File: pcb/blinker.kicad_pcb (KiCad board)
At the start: 2 copper layers, 55.9 x 55.9 mm, 14 parts, among them J1 ISP, U1 ATtiny10-TS

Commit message: Final PCB design?
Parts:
- moved D3 4.73 mm to (165.1, 76.2)
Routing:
- net 5VCC: track 49.6 -> 54.4 mm
- net /LED_R: track 12.4 -> 17.2 mm
- net GND: track 5.32 -> 8.23 mm
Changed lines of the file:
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@@
   )
   (footprint "LED_SMD:LED_0805_2012Metric" (layer "F.Cu")
-    (at 165.2525 80.93)
+    (at 165.1 76.2)
     (descr "LED SMD 0805 (2012 Metric), square (rectangular) end terminal, IPC_7351 nominal, (Body size source: https://docs.google.com/spreadsheets/d/1BsfQQcO9C6DZCsRaXUlFlo91Tg2WpOkGARC1WS5S8t0/edit?usp=sharing), generated with kicad-footprint-generator")
     (tags "LED")
@@
     (fp_line (start 8.471 6.568) (end 8.471 1.44) (layer "B.SilkS") (width 0.12))
     (fp_line (start 10.231 4.854) (end 10.231 -4.854) (layer "B.SilkS") (width 0.12))
+    (fp_line (start 10.991 3.637) (end 10.991 -3.637) (layer "B.SilkS") (width 0.12))
     (fp_line (start 6.311 -1.44) (end 6.311 -7.666) (layer "B.SilkS") (width 0.12))
     (fp_line (start 9.231 5.952) (end 9.231 -5.952) (layer "B.SilkS") (width 0.12))
@@
     (fp_line (start 7.151 7.334) (end 7.151 1.44) (layer "B.SilkS") (width 0.12))
     (fp_line (start 5.951 7.777) (end 5.951 -7.777) (layer "B.SilkS") (width 0.12))
-    (fp_line (start 10.991 3.637) (end 10.991 -3.637) (layer "B.SilkS") (width 0.12))
     (fp_line (start 8.991 6.163) (end 8.991 -6.163) (layer "B.SilkS") (width 0.12))
     (fp_line (start 7.511 7.157) (end 7.511 1.44) (layer "B.SilkS") (width 0.12))
@@
   )
   (segment (start 158.05 93.79) (end 158.05 97.56) (width 0.25) (layer "F.Cu") (net 1))
-  (segment (start 173.38 99.28) (end 172.014511 100.645489) (width 0.25) (layer "F.Cu") (net 2))
-  (segment (start 172.014511 100.645489) (end 168.625489 100.645489) (width 0.25) (layer "F.Cu") (net 2))
+  (segment (start 168.914511 100.454511) (end 168.33 99.87) (width 0.25) (layer "F.Cu") (net 2))
+  (segment (start 172.205489 100.454511) (end 168.914511 100.454511) (width 0.25) (layer "F.Cu") (net 2))
+  (segment (start 173.38 99.28) (end 172.205489 100.454511) (width 0.25) (layer "F.Cu") (net 2))
+  (segment (start 168.33 99.87) (end 165.88 99.87) (width 0.25) (layer "F.Cu") (net 2))
   (segment (start 165.88 101.94) (end 170.84 106.9) (width 0.25) (layer "F.Cu") (net 3))
   (segment (start 165.88 100.82) (end 165.88 101.94) (width 0.25) (layer "F.Cu") (net 3))
@@
   (segment (start 158.05 88.971773) (end 157.48 88.401773) (width 0.25) (layer "F.Cu") (net 9))
   (segment (start 149.86 101.6) (end 149.86 107.178227) (width 0.25) (layer "F.Cu") (net 9))
-  (segment (start 164.315 93.085) (end 164.485 93.255) (width 0.25) (layer "F.Cu") (net 10))
-  (segment (start 164.315 80.93) (end 164.315 93.085) (width 0.25) (layer "F.Cu") (net 10))
+  (segment (start 164.485 93.255) (end 164.485 76.5225) (width 0.25) (layer "F.Cu") (net 10))
+  (segment (start 164.485 76.5225) (end 164.1625 76.2) (width 0.25) (layer "F.Cu") (net 10))
   (segment (start 166.6 108.24) (end 172.04 108.24) (width 0.25) (layer "F.Cu") (net 11))
+  (segment (start 167 91.59) (end 167 77.1625) (width 0.25) (layer "F.Cu") (net 11))
   (segment (start 163.605 99.87) (end 163.221428 99.87) (width 0.25) (layer "F.Cu") (net 11))
+  (segment (start 167 77.1625) (end 166.0375 76.2) (width 0.25) (layer "F.Cu") (net 11))
   (segment (start 162.61798 100.473448) (end 162.61798 104.25798) (width 0.25) (layer "F.Cu") (net 11))
   (segment (start 166.6 108.24) (end 165.75 107.39) (width 0.25) (layer "F.Cu") (net 11))
   (segment (start 162.61798 104.25798) (end 165.75 107.39) (width 0.25) (layer "F.Cu") (net 11))
-  (segment (start 166.19 80.93) (end 167 81.74) (width 0.25) (layer "F.Cu") (net 11))
-  (segment (start 167 81.74) (end 167 91.59) (width 0.25) (layer "F.Cu") (net 11))
   (segment (start 172.04 108.24) (end 173.38 106.9) (width 0.25) (layer "F.Cu") (net 11))
   (segment (start 163.221428 99.87) (end 162.61798 100.473448) (width 0.25) (layer "F.Cu") (net 11))

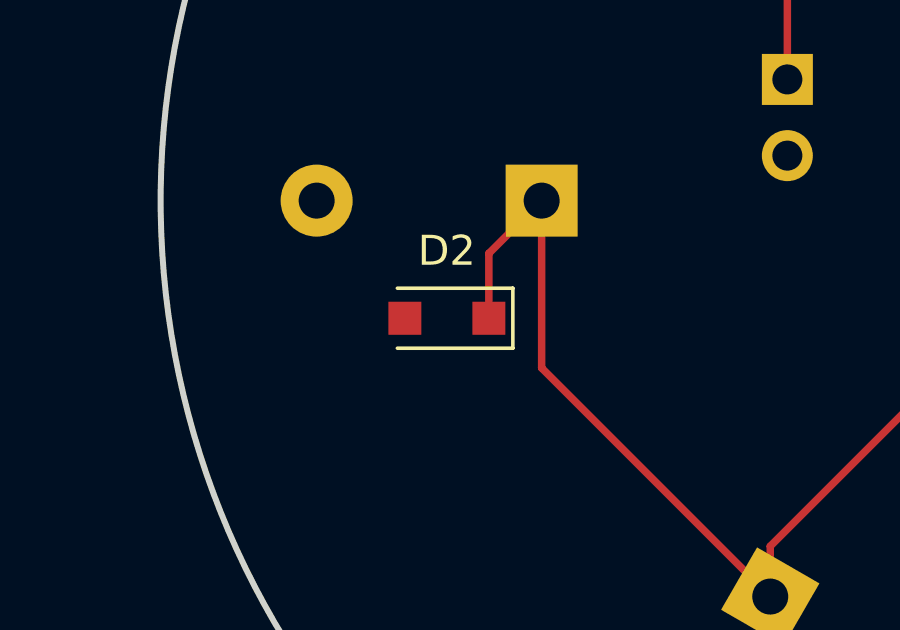
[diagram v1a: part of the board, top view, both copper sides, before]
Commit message: Fix zener selection.
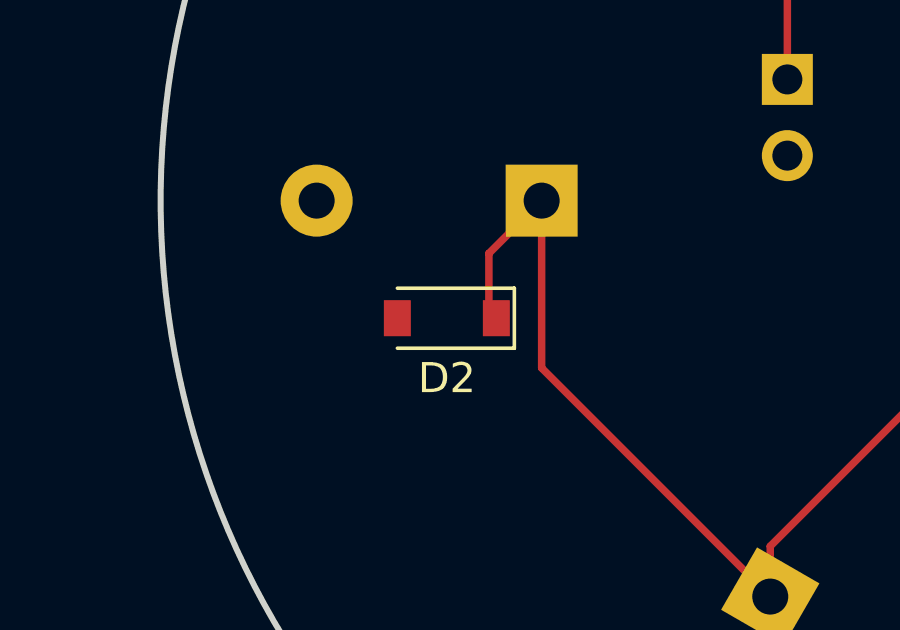
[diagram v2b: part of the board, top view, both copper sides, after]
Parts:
- D2: footprint Diode_SMD:D_SOD-123F -> Diode_SMD:D_SOD-123
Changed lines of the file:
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@@
   (net 11 "5VCC")
   (net 12 "LED")
-  (footprint "Diode_SMD:D_SOD-123F" (layer "F.Cu")
+  (footprint "Diode_SMD:D_SOD-123" (layer "F.Cu")
     (at 146.7 105.52 180)
-    (descr "D_SOD-123F")
-    (tags "D_SOD-123F")
-    (property "LCSC" "C362294")
+    (descr "SOD-123")
+    (tags "SOD-123")
+    (property "LCSC" "C96629")
     (property "Sheetfile" "blinker.kicad_sch")
     (property "Sheetname" "")
     (attr smd)
-    (fp_text reference "D2" (at 0.005 2.245) (layer "F.SilkS")
+    (fp_text reference "D2" (at 0 -2 180) (layer "F.SilkS")
       (effects (font (size 1 1) (thickness 0.15)))
     )
-    (fp_text value "D_Zener" (at 0 2.1) (layer "F.Fab")
+    (fp_text value "D_Zener" (at 0 2.1 180) (layer "F.Fab")
       (effects (font (size 1 1) (thickness 0.15)))
     )
-    (fp_text user "${REFERENCE}" (at -0.127 -1.905) (layer "F.Fab")
+    (fp_text user "${REFERENCE}" (at 0 -2 180) (layer "F.Fab")
       (effects (font (size 1 1) (thickness 0.15)))
     )
-    (fp_line (start -2.2 -1) (end -2.2 1) (layer "F.SilkS") (width 0.12))
-    (fp_line (start -2.2 1) (end 1.65 1) (layer "F.SilkS") (width 0.12))
-    (fp_line (start -2.2 -1) (end 1.65 -1) (layer "F.SilkS") (width 0.12))
-    (fp_line (start -2.2 -1.15) (end -2.2 1.15) (layer "F.CrtYd") (width 0.05))
-    (fp_line (start 2.2 -1.15) (end 2.2 1.15) (layer "F.CrtYd") (width 0.05))
-    (fp_line (start 2.2 1.15) (end -2.2 1.15) (layer "F.CrtYd") (width 0.05))
-    (fp_line (start -2.2 -1.15) (end 2.2 -1.15) (layer "F.CrtYd") (width 0.05))
-    (fp_line (start 0.25 0.4) (end -0.35 0) (layer "F.Fab") (width 0.1))
+    (fp_line (start -2.25 1) (end 1.65 1) (layer "F.SilkS") (width 0.12))
+    (fp_line (start -2.25 -1) (end -2.25 1) (layer "F.SilkS") (width 0.12))
+    (fp_line (start -2.25 -1) (end 1.65 -1) (layer "F.SilkS") (width 0.12))
+    (fp_line (start -2.35 -1.15) (end 2.35 -1.15) (layer "F.CrtYd") (width 0.05))
+    (fp_line (start 2.35 1.15) (end -2.35 1.15) (layer "F.CrtYd") (width 0.05))
+    (fp_line (start 2.35 -1.15) (end 2.35 1.15) (layer "F.CrtYd") (width 0.05))
+    (fp_line (start -2.35 -1.15) (end -2.35 1.15) (layer "F.CrtYd") (width 0.05))
+    (fp_line (start -0.35 0) (end -0.35 0.55) (layer "F.Fab") (width 0.1))
     (fp_line (start -0.35 0) (end 0.25 -0.4) (layer "F.Fab") (width 0.1))
+    (fp_line (start -0.75 0) (end -0.35 0) (layer "F.Fab") (width 0.1))
+    (fp_line (start 1.4 0.9) (end -1.4 0.9) (layer "F.Fab") (width 0.1))
     (fp_line (start -0.35 0) (end -0.35 -0.55) (layer "F.Fab") (width 0.1))
-    (fp_line (start -0.35 0) (end -0.35 0.55) (layer "F.Fab") (width 0.1))
-    (fp_line (start -0.75 0) (end -0.35 0) (layer "F.Fab") (width 0.1))
     (fp_line (start -1.4 -0.9) (end 1.4 -0.9) (layer "F.Fab") (width 0.1))
     (fp_line (start 0.25 -0.4) (end 0.25 0.4) (layer "F.Fab") (width 0.1))
+    (fp_line (start -1.4 0.9) (end -1.4 -0.9) (layer "F.Fab") (width 0.1))
     (fp_line (start 0.25 0) (end 0.75 0) (layer "F.Fab") (width 0.1))
     (fp_line (start 1.4 -0.9) (end 1.4 0.9) (layer "F.Fab") (width 0.1))
-    (fp_line (start 1.4 0.9) (end -1.4 0.9) (layer "F.Fab") (width 0.1))
-    (fp_line (start -1.4 0.9) (end -1.4 -0.9) (layer "F.Fab") (width 0.1))
-    (pad "1" smd rect (at -1.4 0 180) (size 1.1 1.1) (layers "F.Cu" "F.Paste" "F.Mask")
+    (fp_line (start 0.25 0.4) (end -0.35 0) (layer "F.Fab") (width 0.1))
+    (pad "1" smd rect (at -1.65 0 180) (size 0.9 1.2) (layers "F.Cu" "F.Paste" "F.Mask")
       (net 9 "2.7VCC") (pinfunction "K") (pintype "passive"))
-    (pad "2" smd rect (at 1.4 0 180) (size 1.1 1.1) (layers "F.Cu" "F.Paste" "F.Mask")
+    (pad "2" smd rect (at 1.65 0 180) (size 0.9 1.2) (layers "F.Cu" "F.Paste" "F.Mask")
       (net 2 "GND") (pinfunction "A") (pintype "passive"))
-    (model "${KICAD6_3DMODEL_DIR}/Diode_SMD.3dshapes/D_SOD-123F.wrl"
+    (model "${KICAD6_3DMODEL_DIR}/Diode_SMD.3dshapes/D_SOD-123.wrl"
       (offset (xyz 0 0 0))
       (scale (xyz 1 1 1))

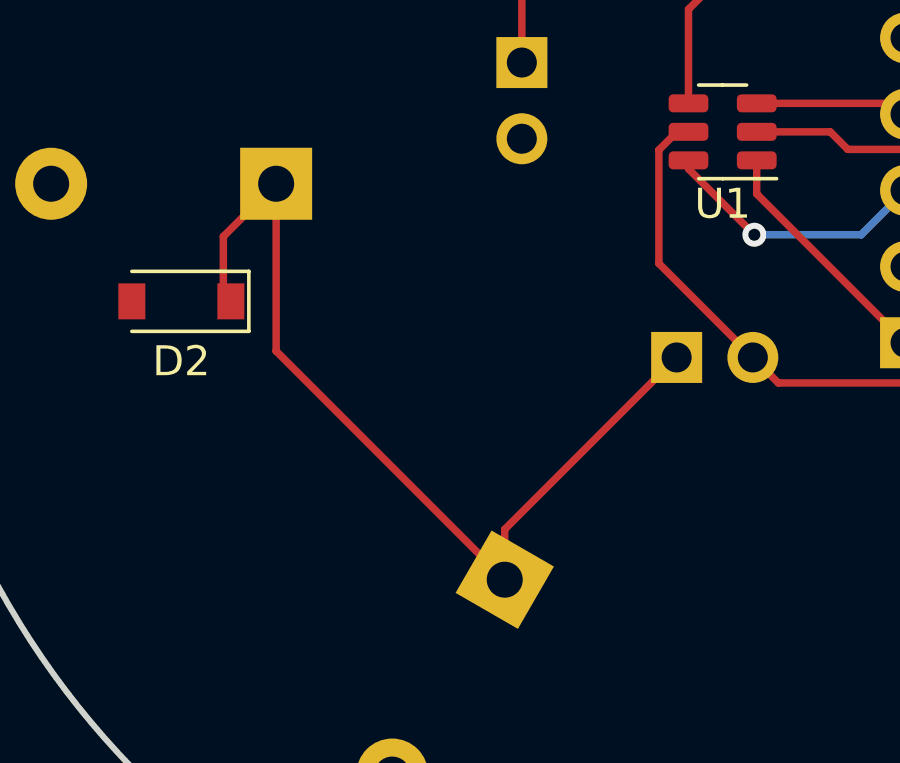
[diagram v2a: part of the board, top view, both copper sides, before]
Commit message: Gotta fix the rotation on U1.
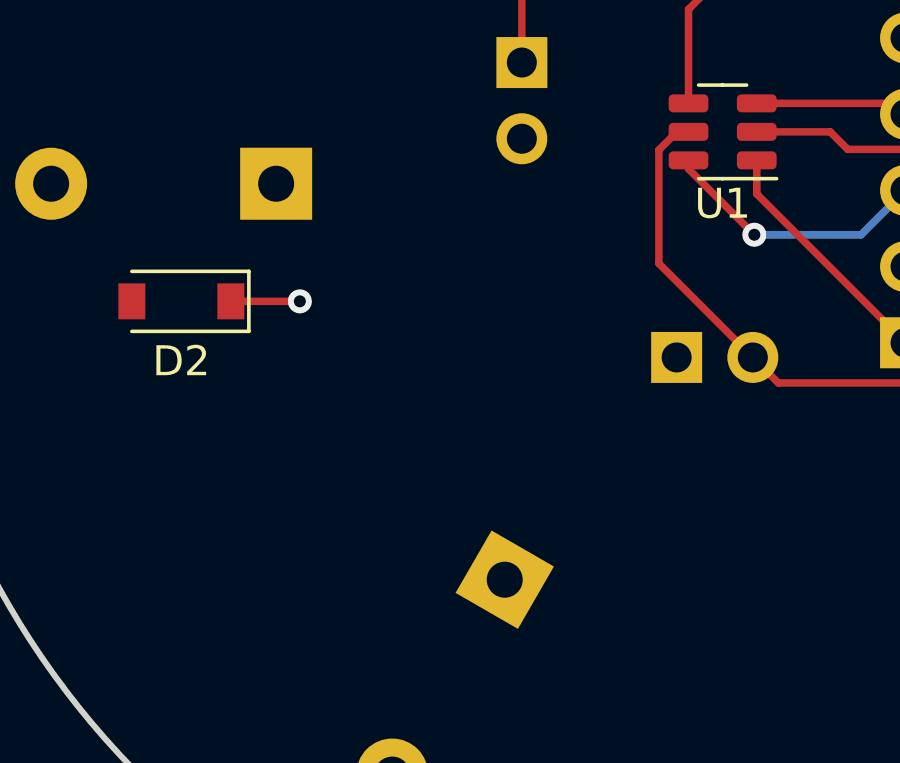
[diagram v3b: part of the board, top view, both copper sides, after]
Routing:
- net 2.7VCC: track 34.3 -> 5.82 mm, vias 0 -> 1
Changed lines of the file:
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@@
   (segment (start 165.88 98.92) (end 170.48 98.92) (width 0.25) (layer "F.Cu") (net 7))
   (segment (start 170.48 98.92) (end 170.84 99.28) (width 0.25) (layer "F.Cu") (net 7))
-  (segment (start 148.1 105.52) (end 148.1 103.36) (width 0.25) (layer "F.Cu") (net 9))
-  (segment (start 157.48 113.12) (end 163.21 107.39) (width 0.25) (layer "F.Cu") (net 9))
   (segment (start 158.05 91.69) (end 158.05 88.971773) (width 0.25) (layer "F.Cu") (net 9))
-  (segment (start 149.86 107.178227) (end 157.48 114.798227) (width 0.25) (layer "F.Cu") (net 9))
-  (segment (start 157.48 114.798227) (end 157.48 113.12) (width 0.25) (layer "F.Cu") (net 9))
-  (segment (start 148.1 103.36) (end 149.86 101.6) (width 0.25) (layer "F.Cu") (net 9))
   (segment (start 158.05 88.971773) (end 157.48 88.401773) (width 0.25) (layer "F.Cu") (net 9))
-  (segment (start 149.86 101.6) (end 149.86 107.178227) (width 0.25) (layer "F.Cu") (net 9))
+  (segment (start 148.35 105.52) (end 150.65 105.52) (width 0.25) (layer "F.Cu") (net 9))
+  (via (at 150.65 105.52) (size 0.8) (drill 0.4) (layers "F.Cu" "B.Cu") (net 9))
   (segment (start 164.485 93.255) (end 164.485 76.5225) (width 0.25) (layer "F.Cu") (net 10))
   (segment (start 164.485 76.5225) (end 164.1625 76.2) (width 0.25) (layer "F.Cu") (net 10))
